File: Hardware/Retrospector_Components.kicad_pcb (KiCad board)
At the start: 4 copper layers, 60 x 110 mm, 149 parts, among them J1 SWD_Header, J2 Eurorack_10_pin_power, J3 Conn_01x08_Male, J4 Conn_01x08_Male, J5 Conn_01x08_Male, J6 Conn_01x08_Male, J7 USB_B_Micro, U1 STM32H743ZITx, U10 LM2675M-5, U11 TL072, U2 IS42S16800F-7TLI, U3 PCM5100APW, U4 AS3364, U5 MCP6004, U6 MCP6004, U7 TL074, U8 LD1117-3.3-4Tab, Y1 8MHz 20pF

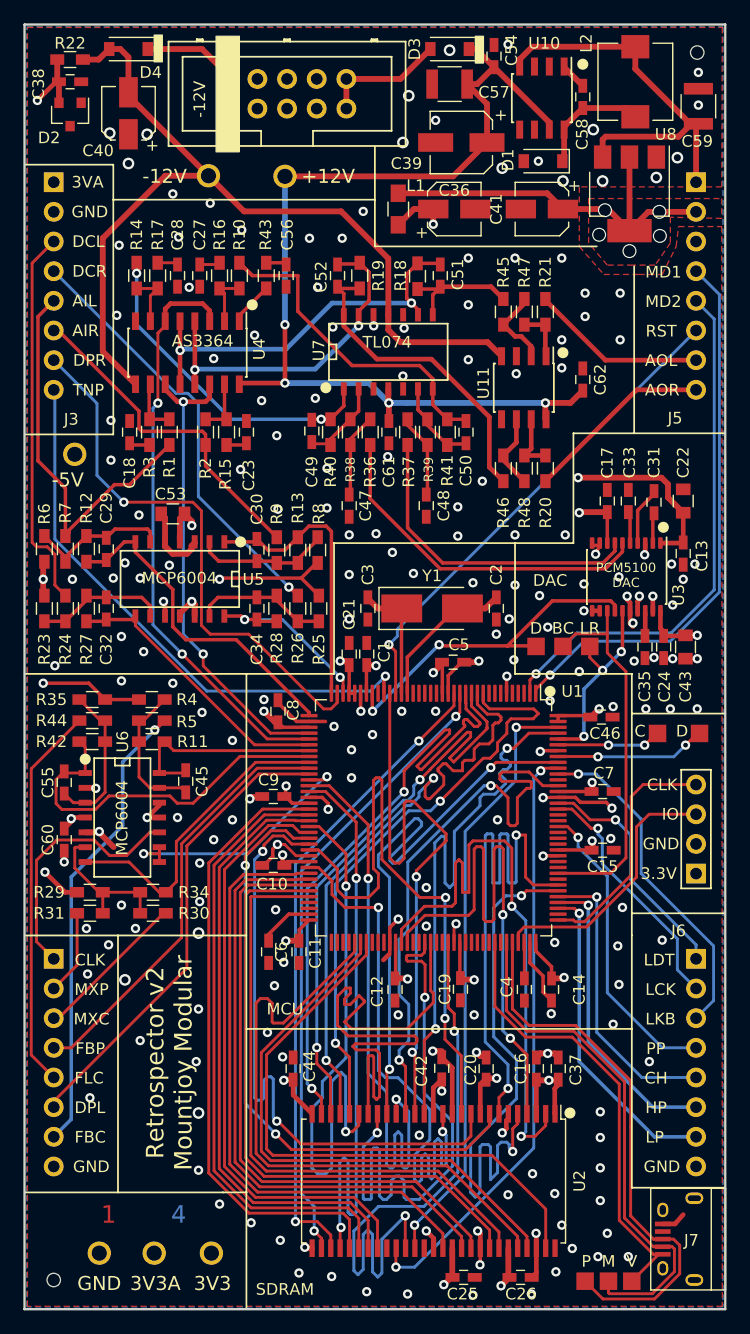
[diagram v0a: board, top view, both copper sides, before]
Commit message: Further clean up to PCB; started work on using SPI for WS2812 LEDs
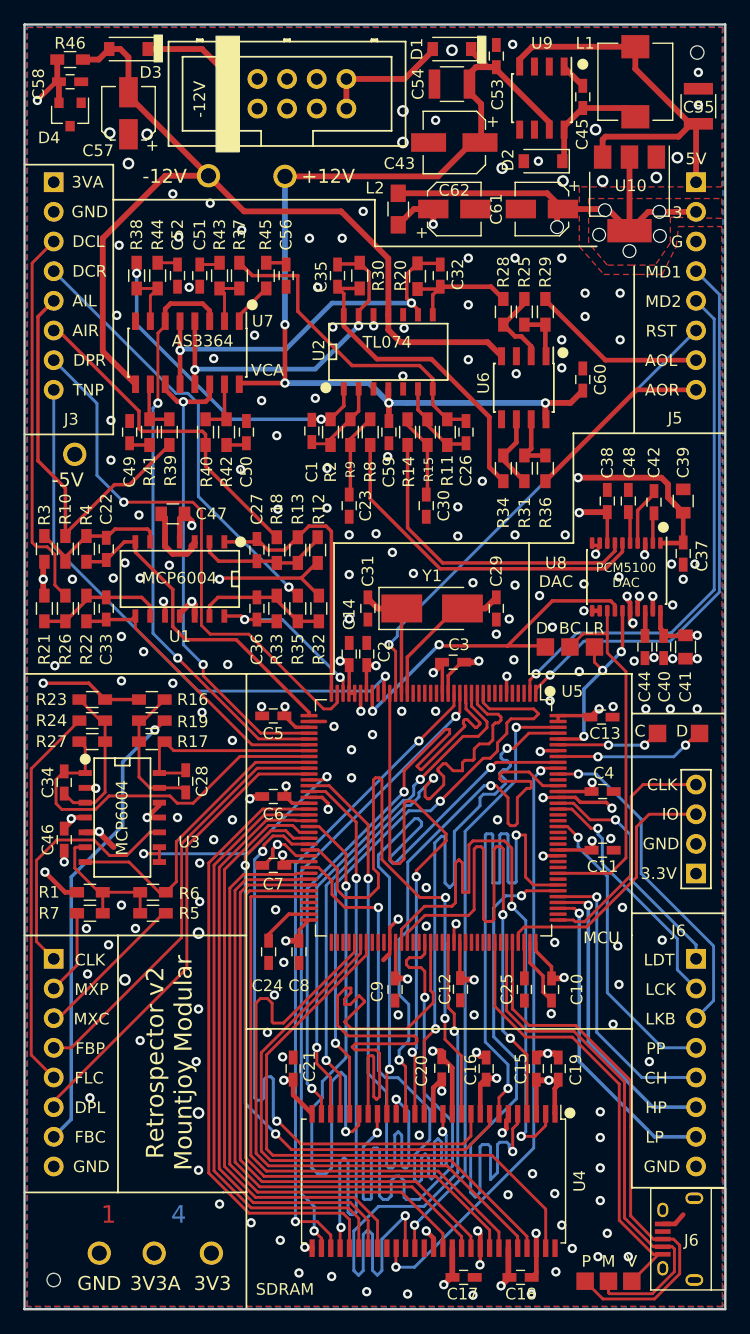
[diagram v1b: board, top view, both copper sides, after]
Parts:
- removed the C9 at (121.3, 116.1)
- added C6: 100nF, Capacitors_SMD:C_0603_HandSoldering, F.Cu at (121.3, 116.1)
- moved TP8 0.80 mm to (144.6, 103.3)
- moved TP9 0.60 mm to (146.7, 103.3)
- moved C43 0.60 mm to (136.8, 60.1)
- moved C5 0.57 mm to (121.3, 109.2), turned to 0 degrees
- moved TP7 0.40 mm to (148.8, 103.3)
- moved C53 0.20 mm to (140.4, 52.7)
- moved C54 0.20 mm to (136.6, 55.1)
- moved D1 0.20 mm to (136.6, 52.1)
- renumbered C49 to C1, C14 to C10, C15 to C11, C19 to C12, C46 to C13, C21 to C14, C16 to C15, C20 to C16, C25 to C17, C26 to C18, C37 to C19, C1 to C2, C42 to C20, C44 to C21, C29 to C22, C47 to C23, C6 to C24, C4 to C25, C50 to C26, C30 to C27, C45 to C28, C2 to C29, C5 to C3, C48 to C30, C3 to C31, C51 to C32, C32 to C33, C55 to C34, C52 to C35, C34 to C36, C13 to C37, C17 to C38, C22 to C39, C7 to C4, C24 to C40, C43 to C41, C31 to C42, C39 to C43, C35 to C44, C58 to C45, C60 to C46, C53 to C47, C33 to C48, C18 to C49, C8 to C5, C23 to C50, C27 to C51, C28 to C52, C54 to C53, C57 to C54, C59 to C55, C40 to C57, C38 to C58, C61 to C59, C62 to C60, C41 to C61, C36 to C62, C10 to C7, C11 to C8, C12 to C9, D3 to D1, D1 to D2, D4 to D3, D2 to D4, J3 to J1, J5 to J2, J4 to J3, J6 to J4, J1 to J5, J7 to J6, J2 to J7, L2 to L1, L1 to L2, R29 to R1, R7 to R10, R41 to R11, R8 to R12, R37 to R14, R39 to R15, R4 to R16, R11 to R17, R9 to R18, R5 to R19, R40 to R2, R18 to R20, R23 to R21, R27 to R22, R35 to R23, R44 to R24, R47 to R25, R24 to R26, R42 to R27, R45 to R28, R21 to R29, R6 to R3, R19 to R30, R48 to R31, R25 to R32, R28 to R33, R46 to R34, R26 to R35, R20 to R36, R10 to R37, R14 to R38, R1 to R39, R12 to R4, R2 to R40, R3 to R41, R15 to R42, R16 to R43, R17 to R44, R43 to R45, R22 to R46, R30 to R5, R34 to R6, R31 to R7, R36 to R8, R38 to R9, U5 to U1, U8 to U10, U7 to U2, U6 to U3, U2 to U4, U1 to U5, U11 to U6, U4 to U7, U3 to U8, U10 to U9
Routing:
- net /FMC_A2: track 50.1 -> 44.1 mm
- net GND: track 87.4 -> 83.9 mm, vias 199 -> 200
- net +3V3: track 115.5 -> 116.2 mm, vias 26 -> 27
- net /DAC_BCLK: track 32.2 -> 31.6 mm
- net /DAC_DATA: track 29.8 -> 30.3 mm
- net /MIX_DRY_CTL: track 40.8 -> 41.3 mm
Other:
- board text added: "3"
- board text added: "5V"
- board text added: "G"
- board text added: "VCA"

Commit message: Updated controls schematic
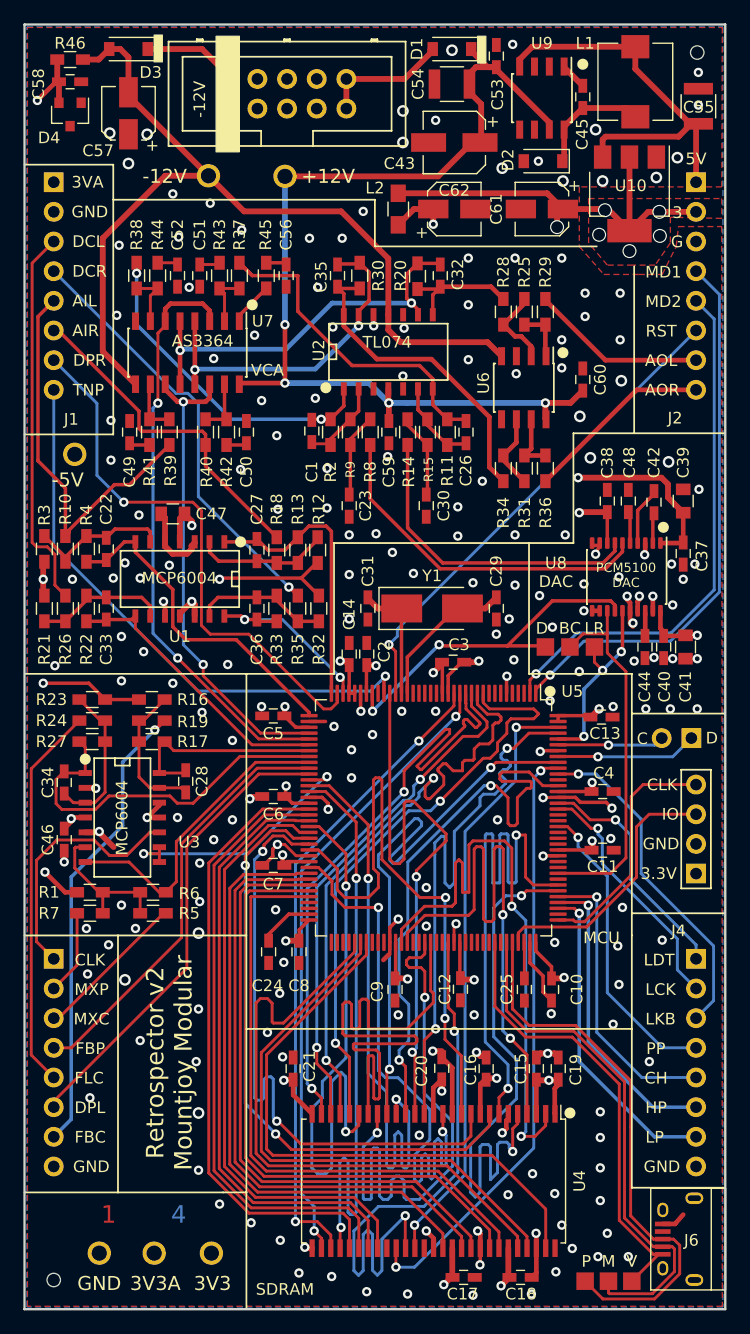
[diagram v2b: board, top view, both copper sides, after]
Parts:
- removed TP13, TP14: TestPoint, Measurement_Points:Measurement_Point_Square-SMD-Pad_Small
- added J8: I2C_TestPoint, Pin_Headers:Pin_Header_Straight_1x02_Pitch2.54mm, F.Cu at (157.1, 111.1)
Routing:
- net /FMC_BA1: track 53.4 -> 51.8 mm
- net /I2C1_SDA: track 13.0 -> 12.1 mm, vias 2 -> 1
- net /I2C1_SCL: track 8.98 -> 9.13 mm, vias 2 -> 1
- net GND: vias 200 -> 205
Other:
- board text added: "J1"
- board text added: "J2"
- board text added: "J4"
- board text removed: "J3"
- board text removed: "J5"
- board text removed: "J6"
- board text removed: "To Do: Ground Vias"

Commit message: WS2812 LEDs tested and working
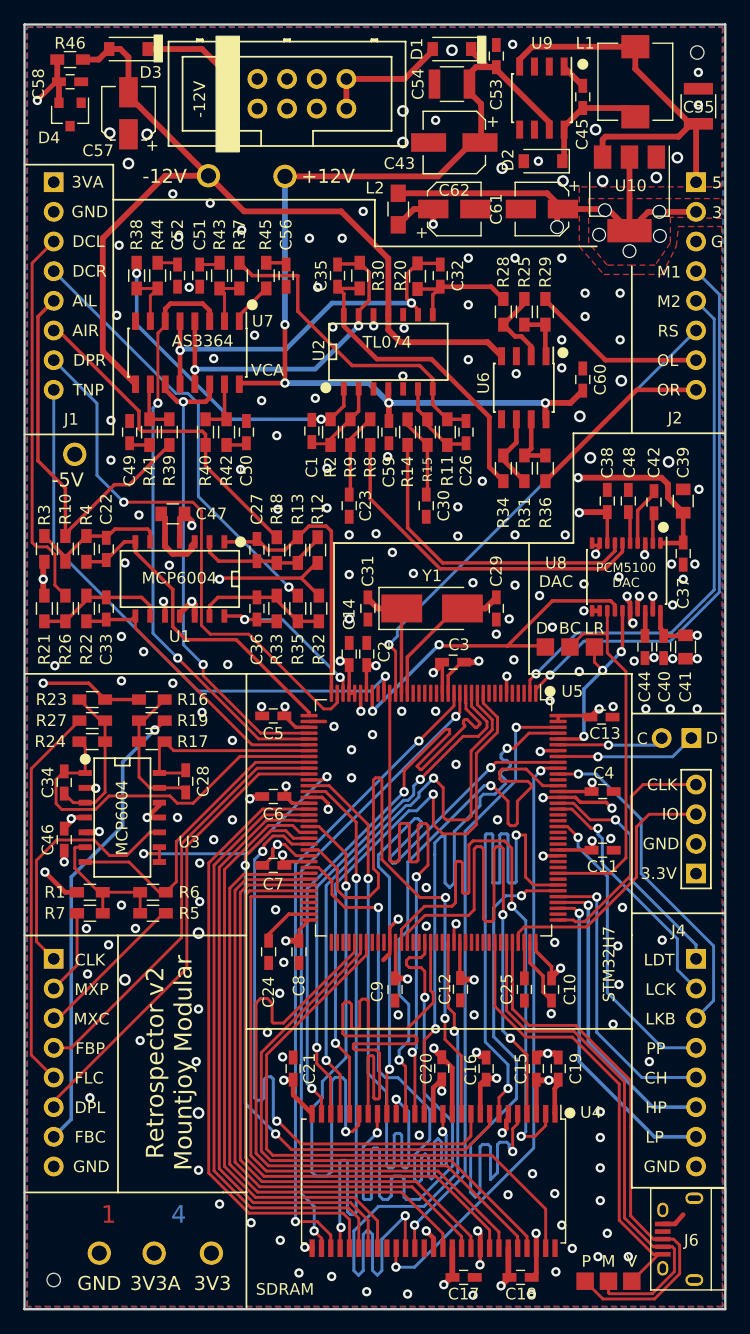
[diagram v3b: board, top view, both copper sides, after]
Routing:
- net /FMC_SD~WE: track 50.6 -> 52.3 mm
- net GND: track 83.9 -> 82.4 mm, vias 205 -> 206
- net /FMC_A0: track 50.5 -> 51.2 mm
- net /-5V_REF: vias 8 -> 5
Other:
- board text added: "5"
- board text added: "M1"
- board text added: "M2"
- board text added: "OL"
- board text added: "OR"
- board text added: "RS"
- board text added: "STM32H7"
- board text removed: "5V"
- board text removed: "AOL"
- board text removed: "AOR"
- board text removed: "MCU"
- board text removed: "MD1"
- board text removed: "MD2"
- board text removed: "RST"

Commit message: Updates to control and panel PCBs
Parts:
- C43: footprint Capacitors_SMD:CP_Elec_5x5.7 -> Capacitors_SMD:CP_Elec_5x5.8
- C61: footprint Capacitors_SMD:CP_Elec_4x5.8 -> Capacitors_SMD:CP_Elec_5x5.8
- moved C61 0.10 mm to (144.2, 65.8)
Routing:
- net +3.3VA: track 35.4 -> 37.8 mm, vias 6 -> 7

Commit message: Update Retrospector_Components.kicad_pcb
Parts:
- moved C34 0.20 mm to (103.2, 114.9)
- moved C46 0.20 mm to (103.2, 119.8)
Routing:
- net GND: track 82.4 -> 87.6 mm, vias 206 -> 216
- net /FILTER_CV_SCALED: track 32.1 -> 33.4 mm

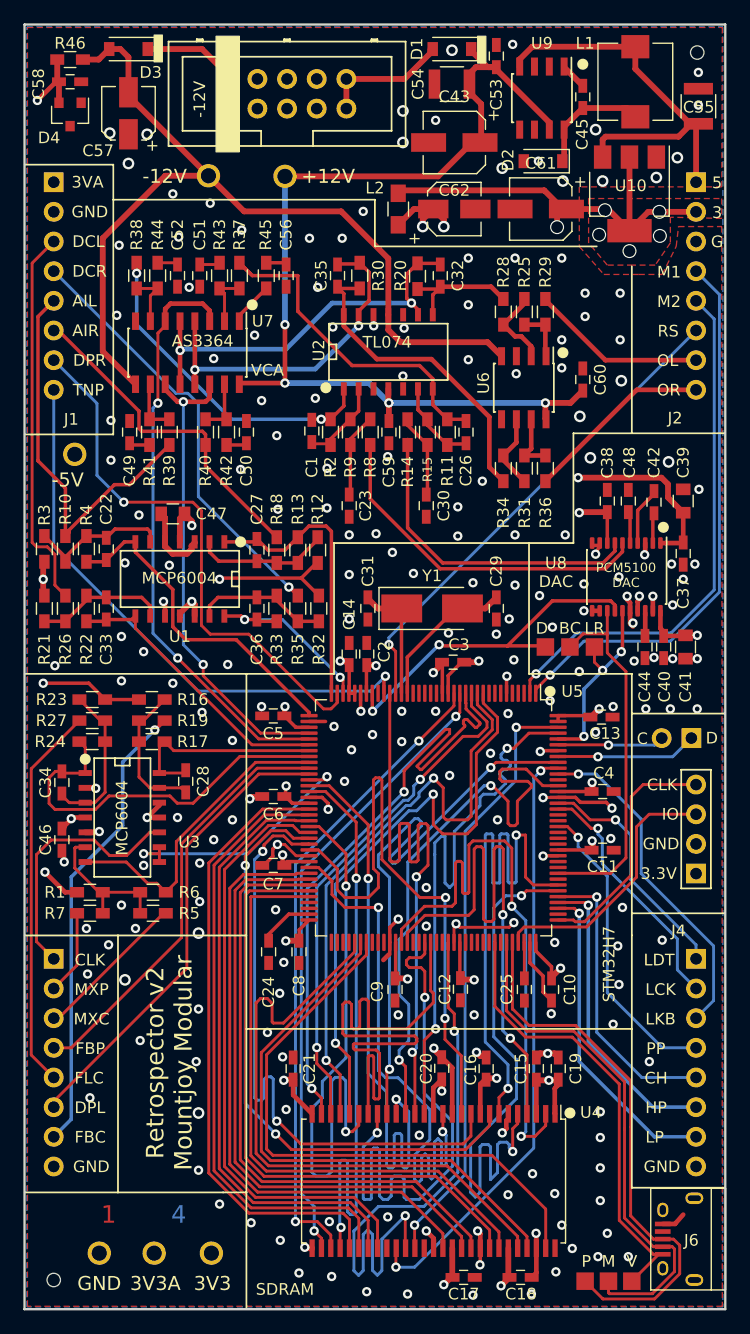
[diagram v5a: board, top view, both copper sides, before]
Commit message: Final updates to v2 PCBs for production; USB DFU Mode working
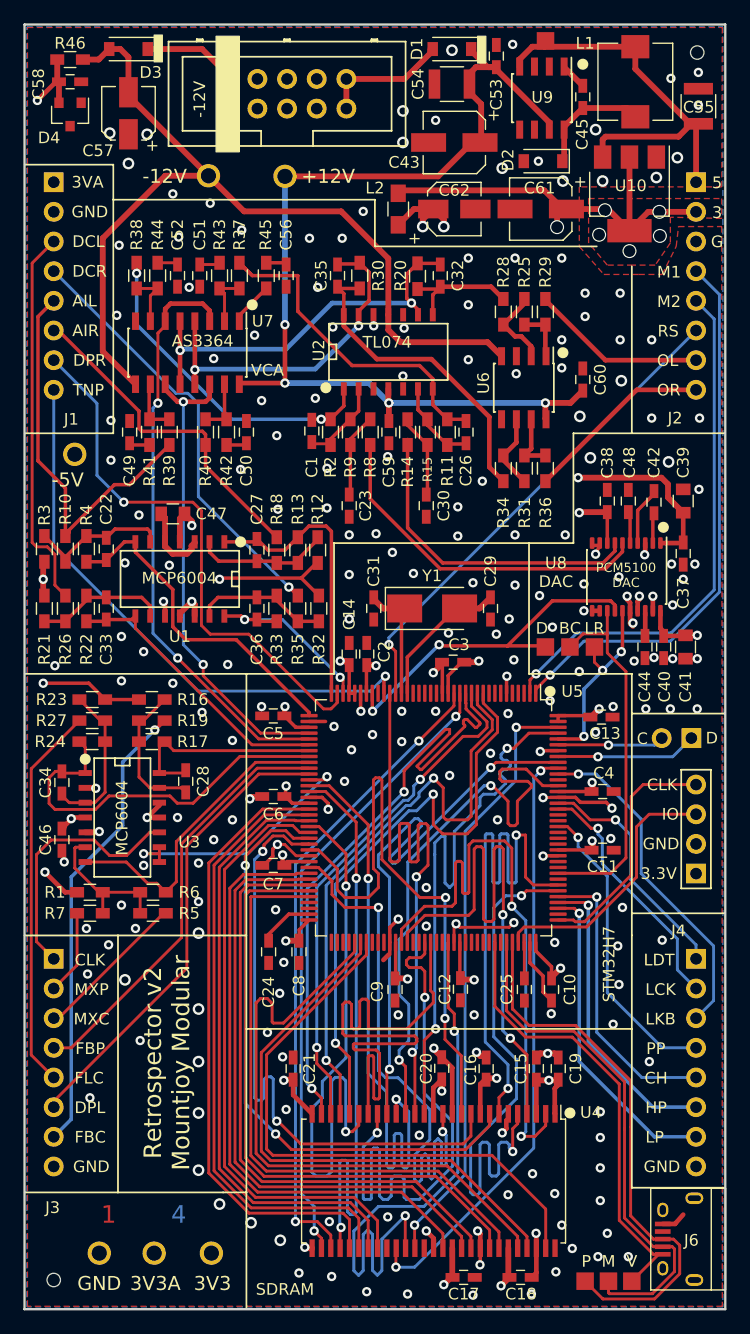
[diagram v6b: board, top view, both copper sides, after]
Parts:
- added TP13: TestPoint, Measurement_Points:Measurement_Point_Square-SMD-Pad_Small, F.Cu at (144.6, 51.4)
- moved C29 0.50 mm to (139.9, 100.0)
- moved C31 0.50 mm to (129.9, 100.0)
- renumbered REF** to 4_Layer_Marker
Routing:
- net +5V: track 35.6 -> 36.1 mm
- net GND: vias 216 -> 220
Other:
- board text added: "J3"

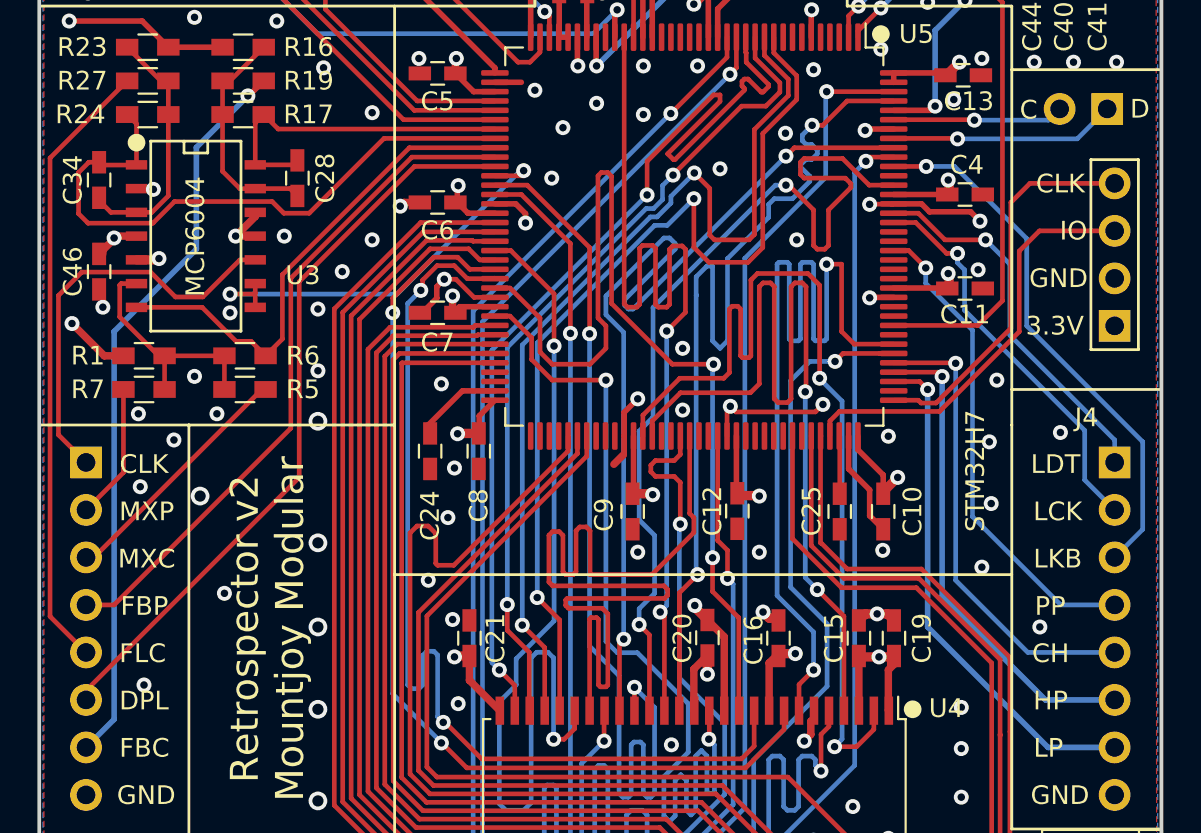
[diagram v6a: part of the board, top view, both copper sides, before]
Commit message: Corrections to PCB for v3; implemented filter mode switch
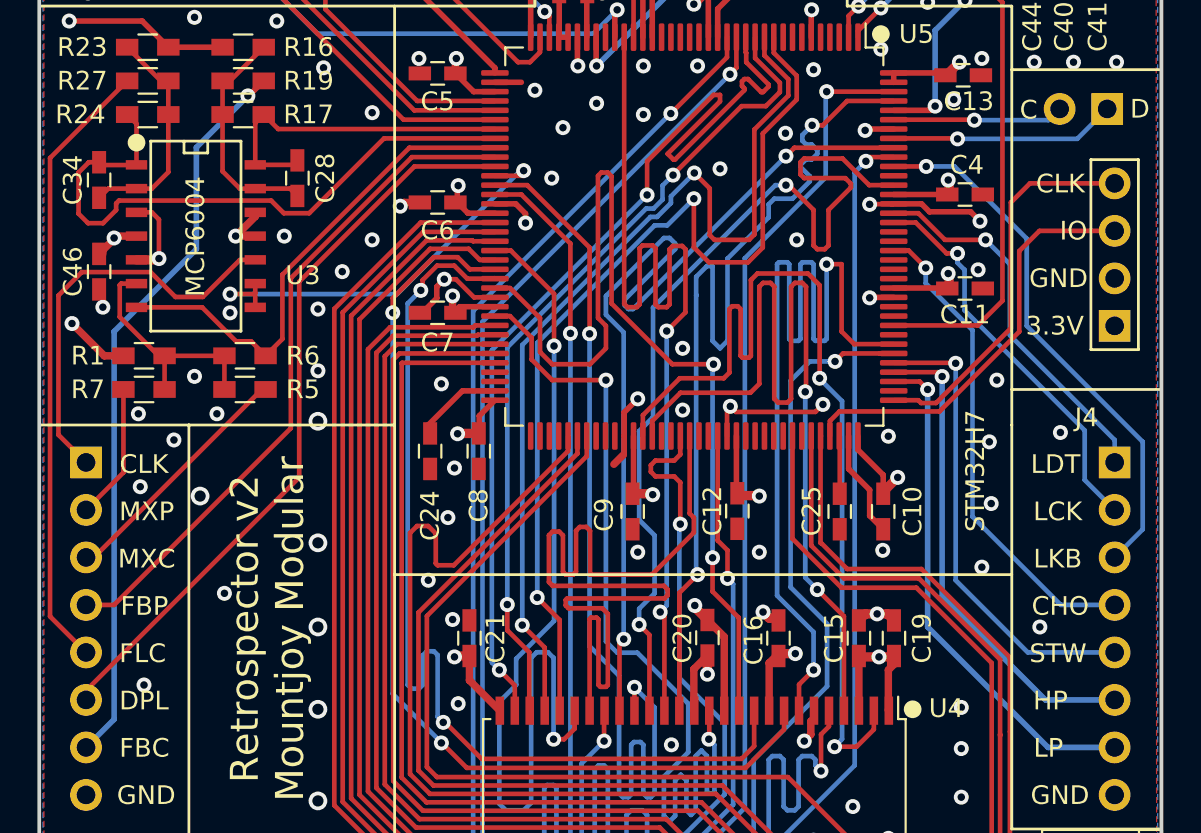
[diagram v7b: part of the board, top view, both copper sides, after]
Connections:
- J4 pad 4: /PINGPONG -> /CHORUS
- J4 pad 5: /CHORUS -> /STEREO_WIDE
- U3 pad 2: GND -> Net-(C34-Pad2)
- U3 pad 3: Net-(C34-Pad2) -> GND
- U5 pad 113: /CHORUS -> /STEREO_WIDE
- U5 pad 125: /PINGPONG -> /CHORUS
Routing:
- net /PINGPONG: track 26.0 -> 0.00 mm, vias 1 -> 0
- net /STEREO_WIDE: track 0.00 -> 25.1 mm, vias 0 -> 1
- net GND: track 87.6 -> 90.2 mm, vias 220 -> 219
- net Net-(C34-Pad2): track 13.5 -> 12.4 mm
- net /CHORUS: track 25.1 -> 26.0 mm
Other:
- board text added: "CHO"
- board text added: "STW"
- board text removed: "CH"
- board text removed: "PP"

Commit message: Updated SDRAM to work with 32MB RAM (implemented A12 line); attempts to get SPI DMA working for LED controller
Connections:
- U4 pad 36: Net-(U4-Pad36) -> /FMC_A12
- U5 pad 87: Net-(U5-Pad87) -> /FMC_A12
